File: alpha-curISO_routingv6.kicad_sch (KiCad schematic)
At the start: 24 parts, among them J2 SWD, U1 RP2040, U5 74AHCT1G125

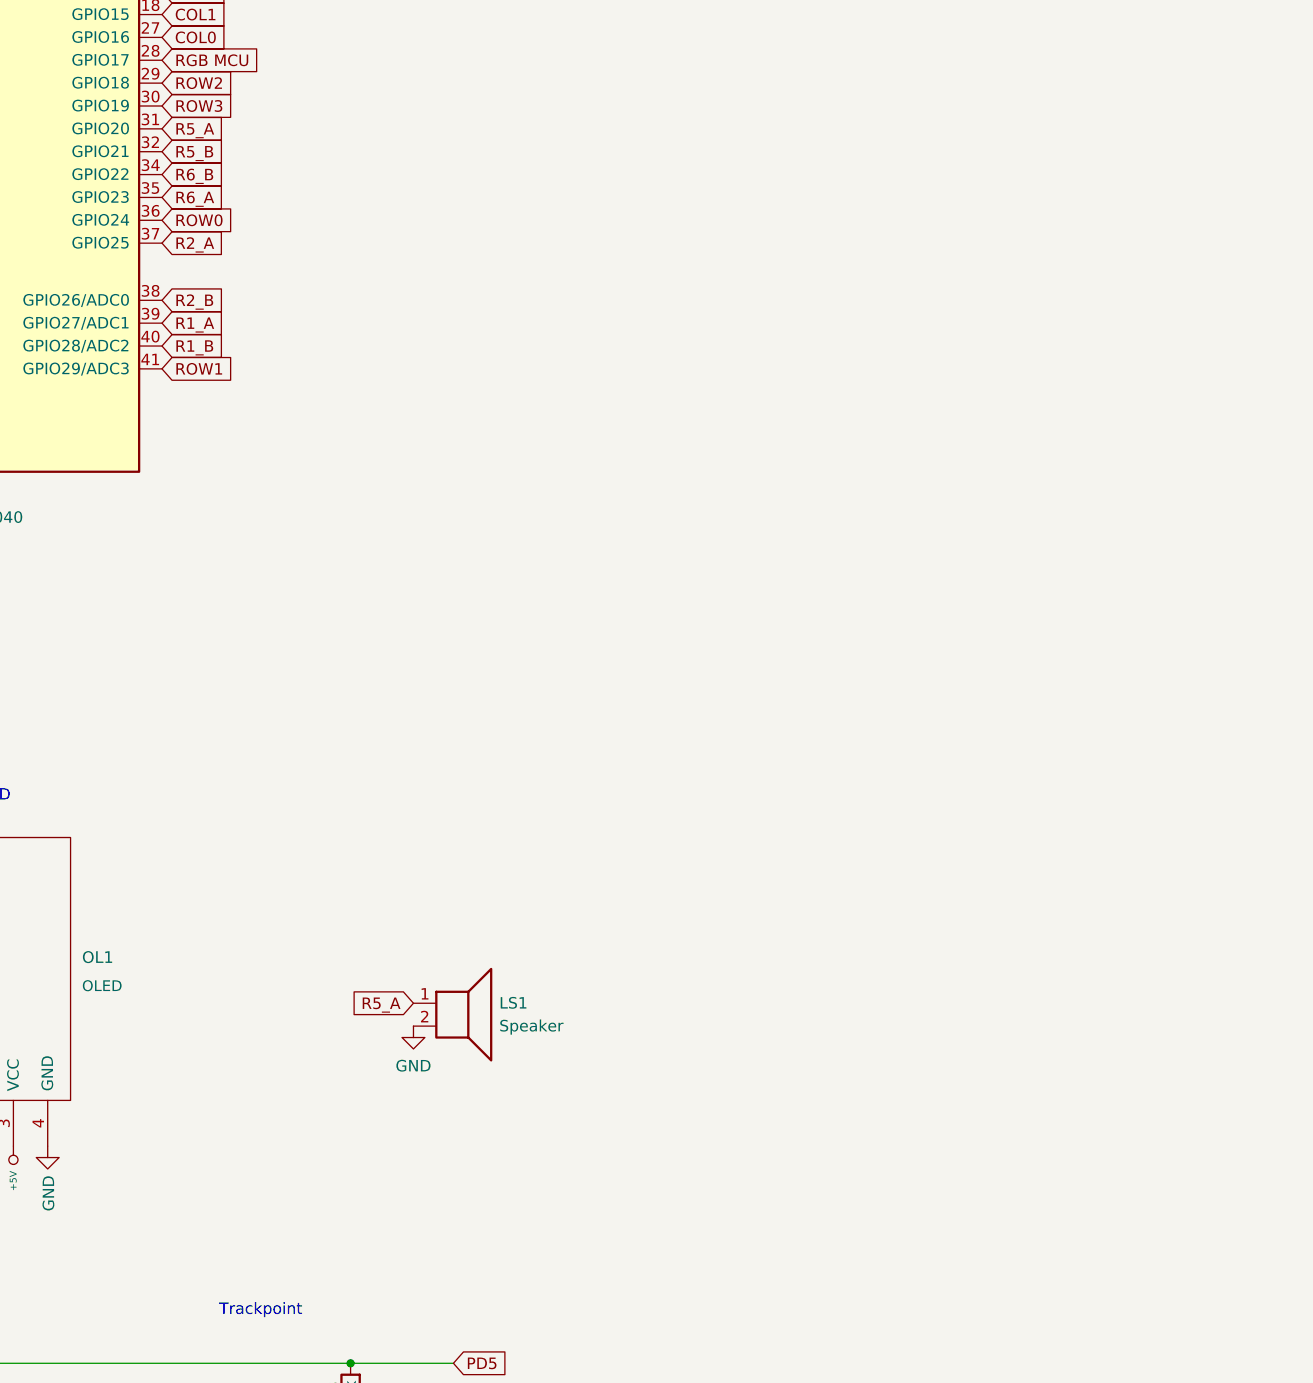
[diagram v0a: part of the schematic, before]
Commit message: catching up with the progress made in 7
catching up work, setting up pcb for round traces, and octagonal pads if desired
implemented complex speakers
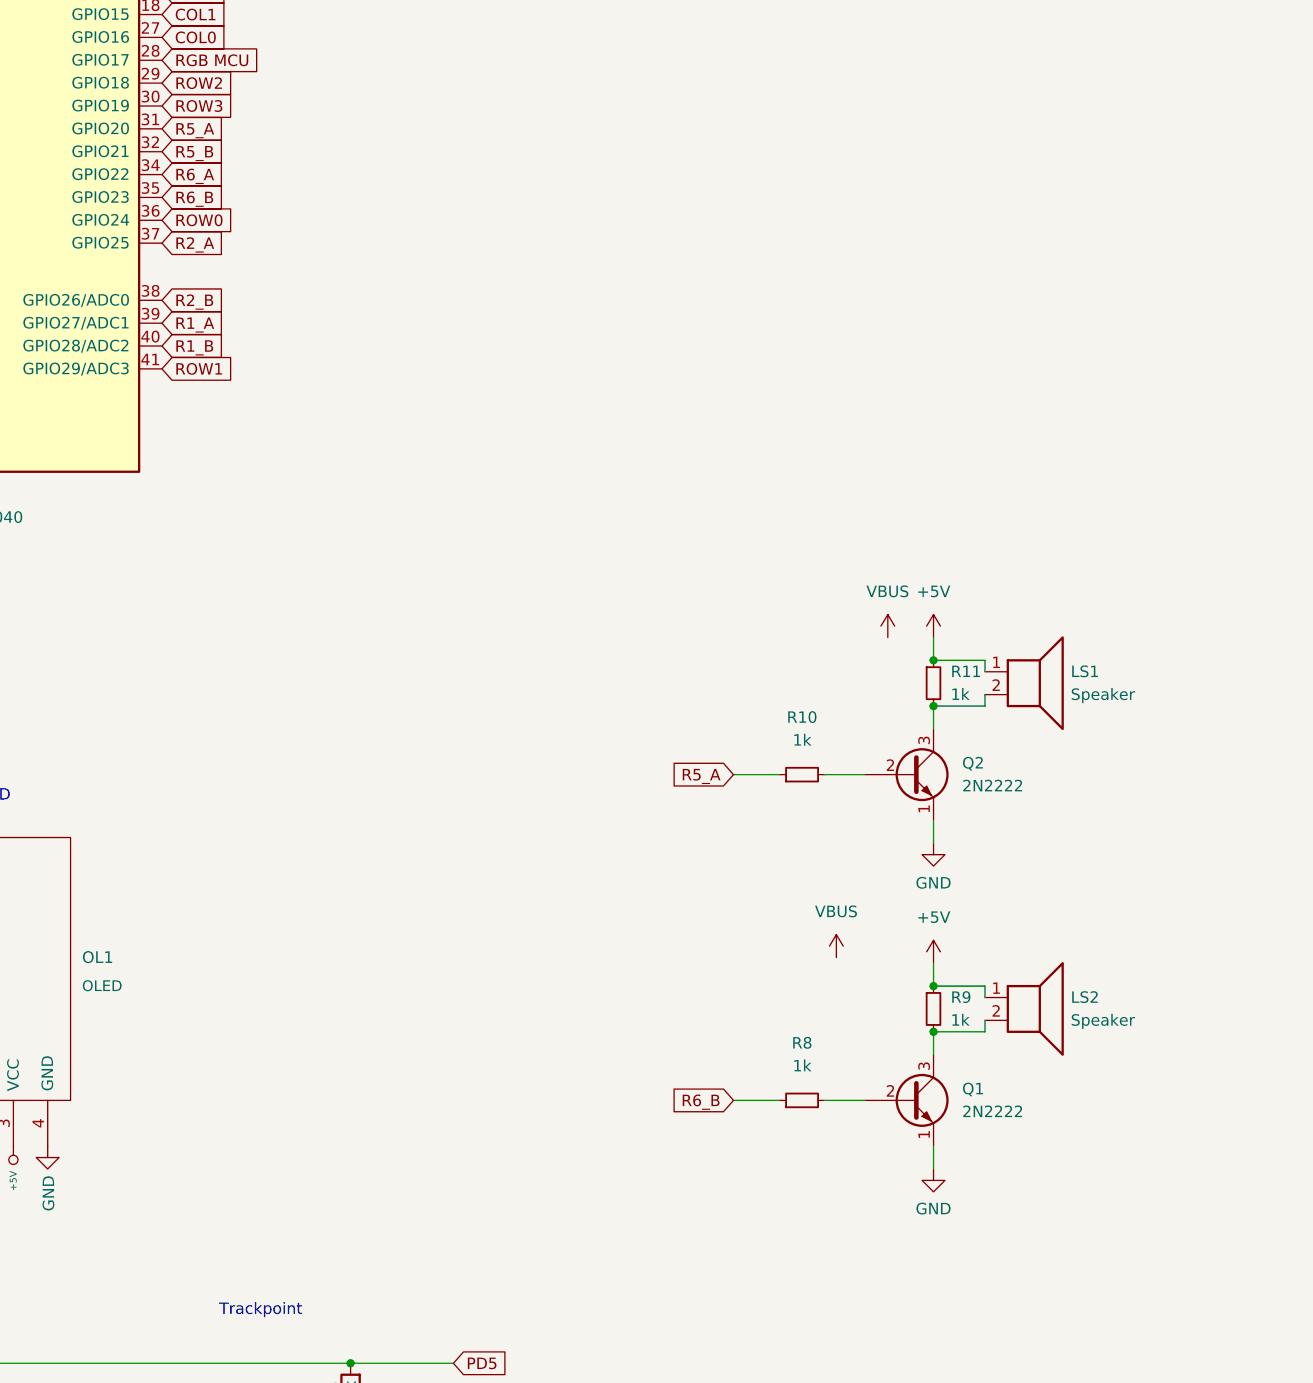
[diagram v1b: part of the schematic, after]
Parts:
- added LS2: Speaker, Keebio-Parts:AST1109MLTRQ, symbol Device:Speaker
- added Q1, Q2: 2N2222, Package_TO_SOT_SMD:SOT-23, symbol Transistor_BJT:2N2219
- added R10, R8: 1k, Keebio-Parts:Diode-Hybrid-Back, symbol Device:R_Small
- added R11, R9: 1k, Resistor_SMD:R_0402_1005Metric, symbol Device:R_Small
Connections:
- net +5V: now also LS1.1, LS2.1, R11.1, R9.1
- net GND: now also Q1.1 (E), Q2.1 (E); no longer LS1.2
- net R5_A: now also R10.1; no longer LS1.1
- net R6_A: now also U1.34 (GPIO22); no longer U1.35 (GPIO23)
- net R6_B: now also U1.35 (GPIO23), R8.1; no longer U1.34 (GPIO22)
- new net: Q2.2 (B), R10.2
- new net: LS1.2, Q2.3 (C), R11.2
- new net: Q1.2 (B), R8.2
- new net: LS2.2, Q1.3 (C), R9.2

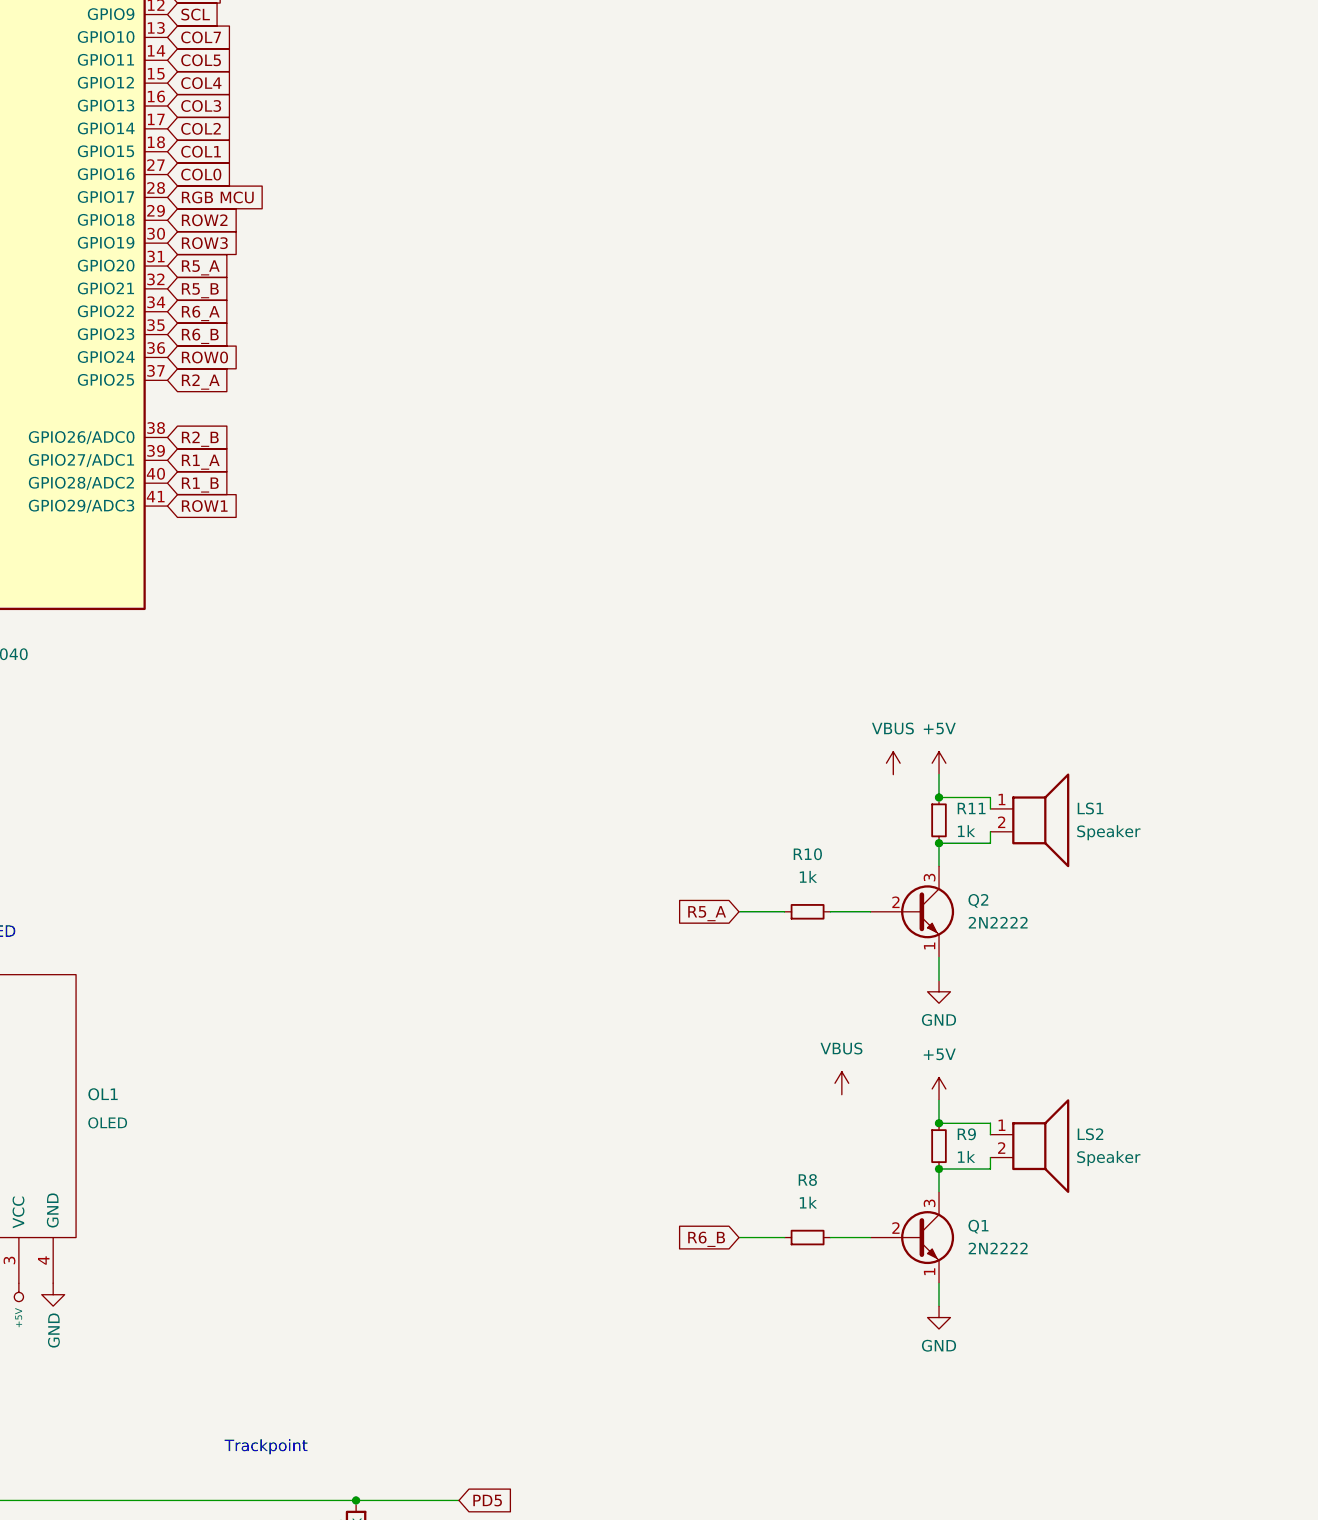
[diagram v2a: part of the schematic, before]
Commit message: finished prototype pcb
missing silkscreen, production files
needs clarification of some errors
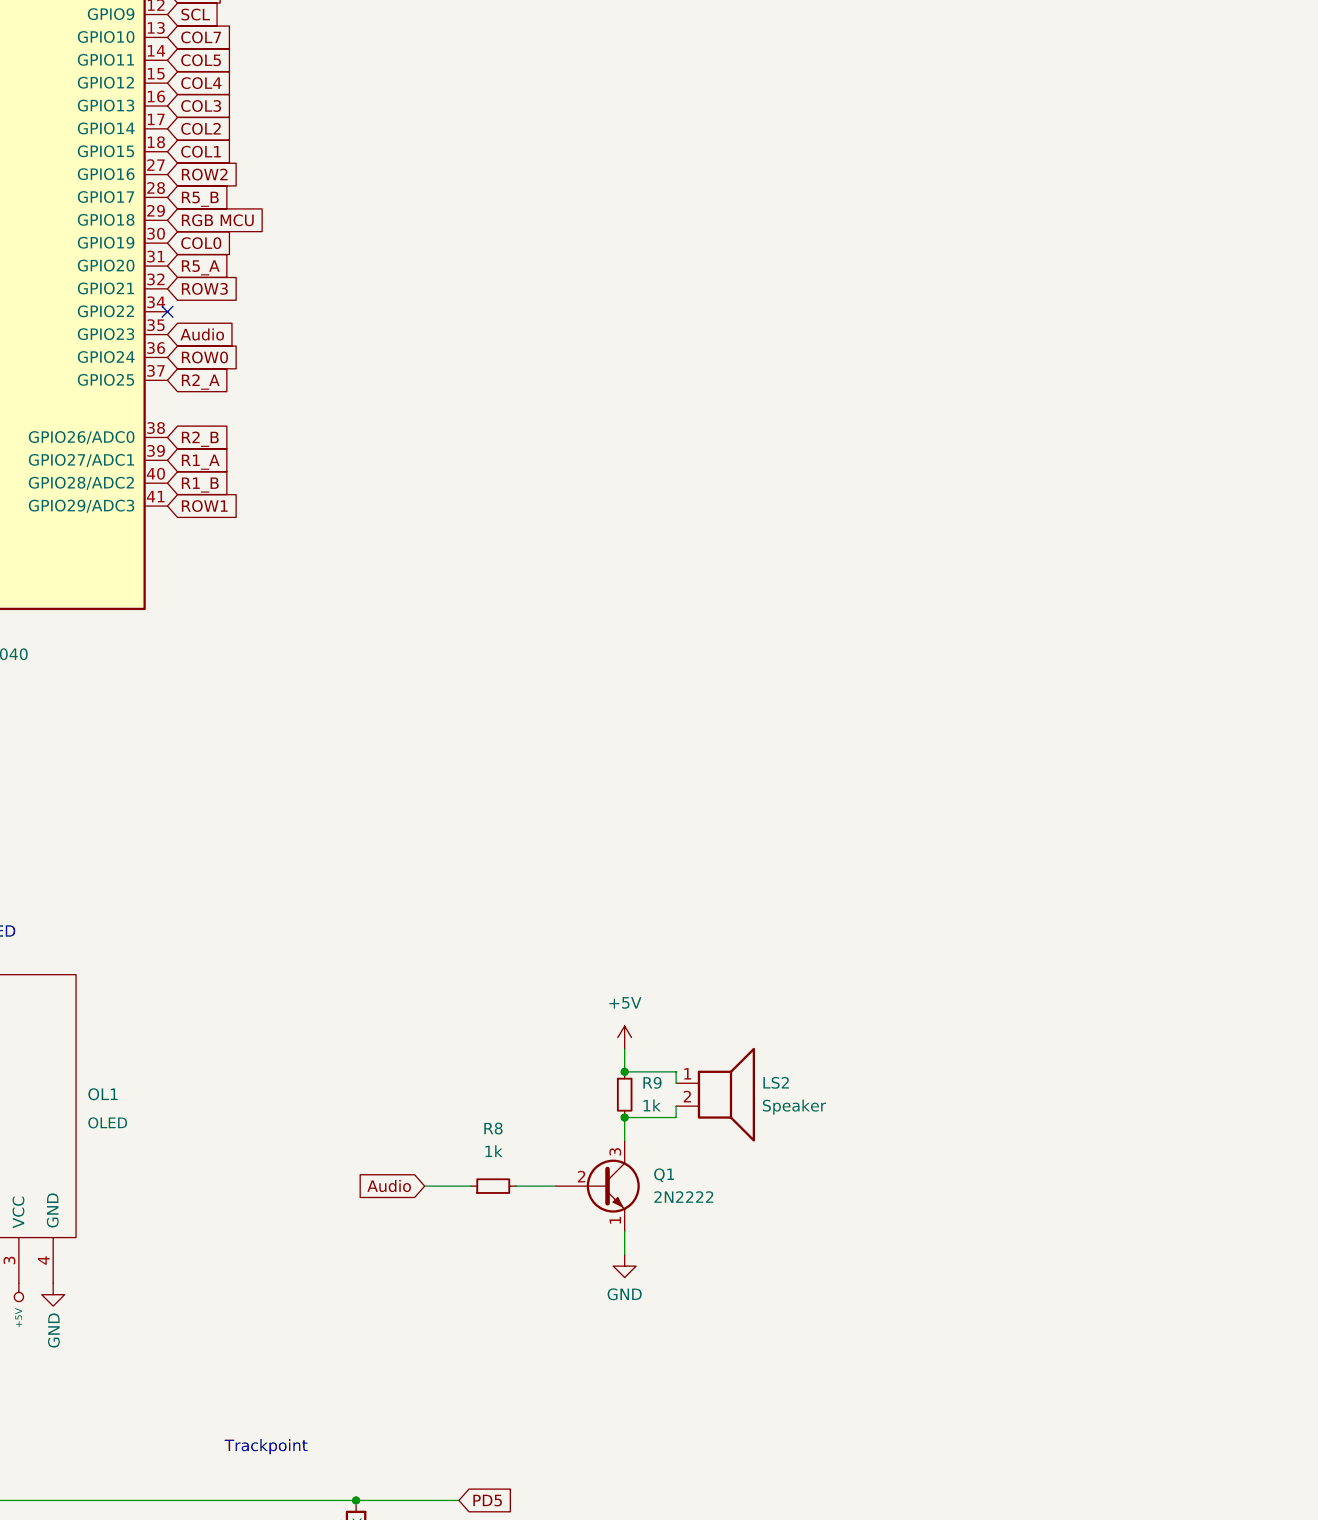
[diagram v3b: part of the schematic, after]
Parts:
- removed LS1: Speaker, Keebio-Parts:AST1109MLTRQ, symbol Device:Speaker
- removed Q2: 2N2222, Package_TO_SOT_SMD:SOT-23, symbol Transistor_BJT:2N2219
- removed R10: 1k, Keebio-Parts:Diode-Hybrid-Back, symbol Device:R_Small
- removed R11: 1k, Resistor_SMD:R_0402_1005Metric, symbol Device:R_Small
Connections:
- net COL0: now also U1.30 (GPIO19); no longer U1.27 (GPIO16)
- net R5_B: now also U1.28 (GPIO17); no longer U1.32 (GPIO21)
- net RGB MCU: now also U1.29 (GPIO18); no longer U1.28 (GPIO17)
- net ROW2: now also U1.27 (GPIO16); no longer U1.29 (GPIO18)
- net ROW3: now also U1.32 (GPIO21); no longer U1.30 (GPIO19)
- net R6_A: no longer names the net of U1.34 (GPIO22)
- net R6_B renamed Audio
- no-connect marks 0 -> 1
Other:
- moved on the sheet: LS2, Q1, R8, R9

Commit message: changed nets a bit
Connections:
- net Audio: now also U1.34 (GPIO22); no longer U1.35 (GPIO23)
- net R1_A: now also U1.38 (GPIO26/ADC0); no longer U1.39 (GPIO27/ADC1)
- net R1_B: now also U1.39 (GPIO27/ADC1); no longer U1.40 (GPIO28/ADC2)
- net R2_A: now also U1.36 (GPIO24); no longer U1.37 (GPIO25)
- net R2_B: now also U1.37 (GPIO25); no longer U1.38 (GPIO26/ADC0)
- net ROW0: now also U1.35 (GPIO23); no longer U1.36 (GPIO24)
- net ROW1: now also U1.40 (GPIO28/ADC2); no longer U1.41 (GPIO29/ADC3)
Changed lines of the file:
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@@
   (junction (at 302.895 170.18) (diameter 0) (color 0 0 0 0)
   )
-  (no_connect (at 80.01 92.71))
+  (no_connect (at 80.01 114.3))
   (wire (pts (xy 298.45 243.84) (xy 315.595 243.84))
     (stroke (width 0) (type default) (color 0 0 0 0))
@@
     )
   )
-  (global_label "R2_B" (shape input) (at 80.01 106.68 0) (fields_autoplaced)
-    (effects (font (size 1.27 1.27)) (justify left))
-    (property "Intersheet References" "${INTERSHEET_REFS}" (id 0) (at 87.1402 106.7594 0)
+  (global_label "R2_B" (shape input) (at 80.01 100.33 0) (fields_autoplaced)
+    (effects (font (size 1.27 1.27)) (justify left))
+    (property "Intersheet References" "${INTERSHEET_REFS}" (id 0) (at 87.1402 100.4094 0)
       (effects (font (size 1.27 1.27)) (justify left) hide)
     )
@@
     )
   )
-  (global_label "ROW1" (shape input) (at 80.01 114.3 0) (fields_autoplaced)
-    (effects (font (size 1.27 1.27)) (justify left))
-    (property "Intersheet References" "${INTERSHEET_REFS}" (id 0) (at 87.6845 114.3794 0)
+  (global_label "ROW1" (shape input) (at 80.01 111.76 0) (fields_autoplaced)
+    (effects (font (size 1.27 1.27)) (justify left))
+    (property "Intersheet References" "${INTERSHEET_REFS}" (id 0) (at 87.6845 111.8394 0)
       (effects (font (size 1.27 1.27)) (justify left) hide)
     )
@@
     )
   )
-  (global_label "R2_A" (shape input) (at 80.01 100.33 0) (fields_autoplaced)
-    (effects (font (size 1.27 1.27)) (justify left))
-    (property "Intersheet References" "${INTERSHEET_REFS}" (id 0) (at 86.9588 100.4094 0)
+  (global_label "R2_A" (shape input) (at 80.01 97.79 0) (fields_autoplaced)
+    (effects (font (size 1.27 1.27)) (justify left))
+    (property "Intersheet References" "${INTERSHEET_REFS}" (id 0) (at 86.9588 97.8694 0)
       (effects (font (size 1.27 1.27)) (justify left) hide)
     )
@@
     )
   )
-  (global_label "ROW0" (shape input) (at 80.01 97.79 0) (fields_autoplaced)
-    (effects (font (size 1.27 1.27)) (justify left))
-    (property "Intersheet References" "${INTERSHEET_REFS}" (id 0) (at 87.6845 97.8694 0)
+  (global_label "ROW0" (shape input) (at 80.01 95.25 0) (fields_autoplaced)
+    (effects (font (size 1.27 1.27)) (justify left))
+    (property "Intersheet References" "${INTERSHEET_REFS}" (id 0) (at 87.6845 95.3294 0)
       (effects (font (size 1.27 1.27)) (justify left) hide)
     )
@@
     )
   )
-  (global_label "Audio" (shape input) (at 80.01 95.25 0) (fields_autoplaced)
-    (effects (font (size 1.27 1.27)) (justify left))
-    (property "Intersheet References" "${INTERSHEET_REFS}" (id 0) (at 87.5636 95.3294 0)
+  (global_label "Audio" (shape input) (at 80.01 92.71 0) (fields_autoplaced)
+    (effects (font (size 1.27 1.27)) (justify left))
+    (property "Intersheet References" "${INTERSHEET_REFS}" (id 0) (at 87.5636 92.7894 0)
       (effects (font (size 1.27 1.27)) (justify left) hide)
     )
@@
     )
   )
-  (global_label "R1_A" (shape input) (at 80.01 109.22 0) (fields_autoplaced)
-    (effects (font (size 1.27 1.27)) (justify left))
-    (property "Intersheet References" "${INTERSHEET_REFS}" (id 0) (at 86.9588 109.2994 0)
+  (global_label "R1_A" (shape input) (at 80.01 106.68 0) (fields_autoplaced)
+    (effects (font (size 1.27 1.27)) (justify left))
+    (property "Intersheet References" "${INTERSHEET_REFS}" (id 0) (at 86.9588 106.7594 0)
       (effects (font (size 1.27 1.27)) (justify left) hide)
     )
@@
     )
   )
-  (global_label "R1_B" (shape input) (at 80.01 111.76 0) (fields_autoplaced)
-    (effects (font (size 1.27 1.27)) (justify left))
-    (property "Intersheet References" "${INTERSHEET_REFS}" (id 0) (at 87.1402 111.8394 0)
-      (effects (font (size 1.27 1.27)) (justify left) hide)
-    )
+  (global_label "R1_B" (shape input) (at 80.01 109.22 0) (fields_autoplaced)
+    (effects (font (size 1.27 1.27)) (justify left))
+    (property "Intersheet References" "${INTERSHEET_REFS}" (id 0) (at 87.1402 109.2994 0)
+      (effects (font (size 1.27 1.27)) (justify left) hide)
+    )
